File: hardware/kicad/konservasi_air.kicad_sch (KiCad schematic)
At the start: 29 parts, among them J1 ADS1115, J10 PUMP, J11 DC_IN_TERMINAL, J12 ESP_GPIO_LEFT, J13 ESP_GPIO_RIGHT, J2 DS18B20, J3 TDS, J4 TURBIDITY, J5 pH, J6 SERVO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

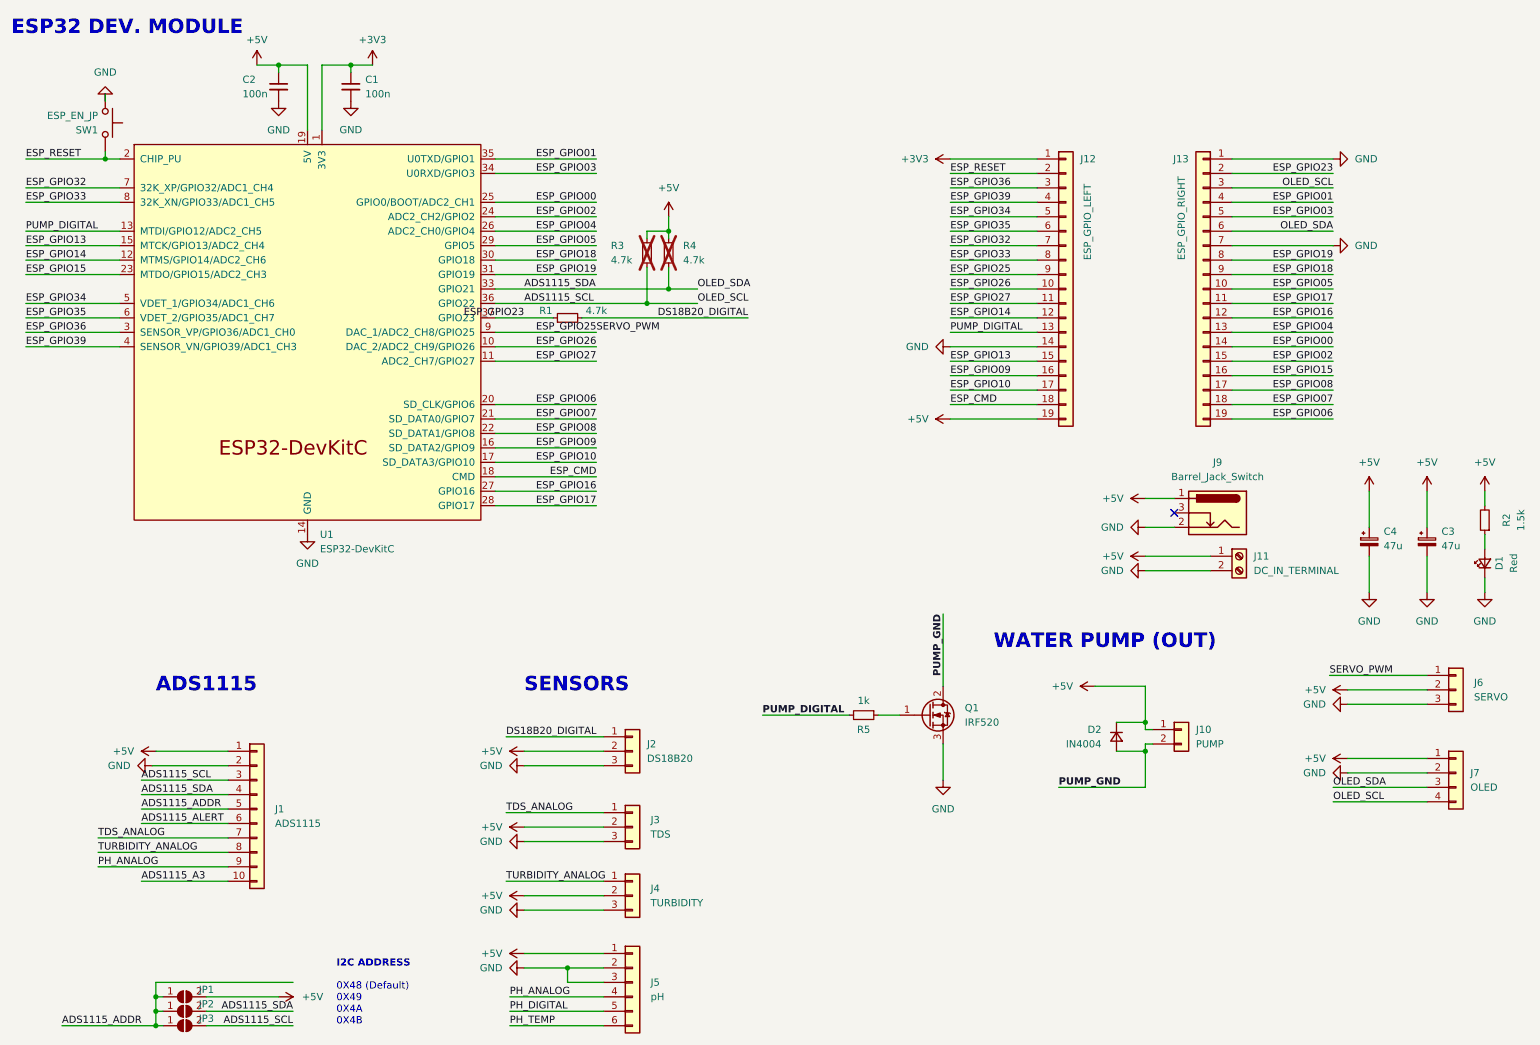
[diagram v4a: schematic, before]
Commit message: Fix Pullup for Temp Sensor
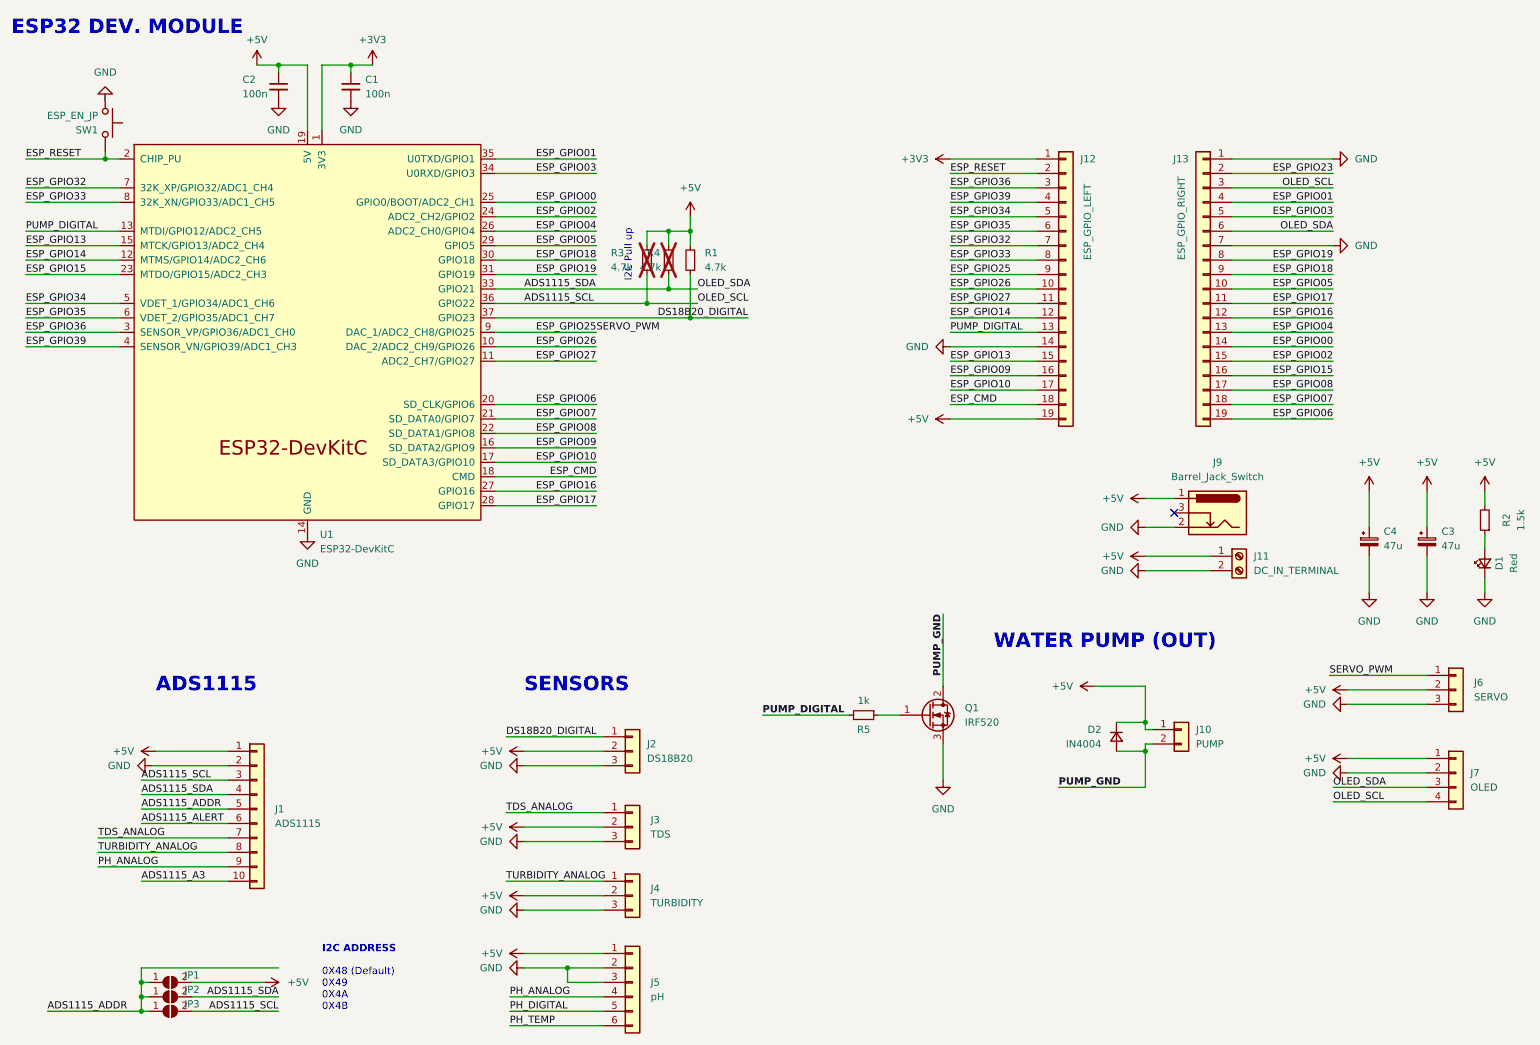
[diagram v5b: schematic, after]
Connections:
- net +5V: now also R1.2
- net DS18B20_DIGITAL: now also R1.1, U1.37 (GPIO23); no longer R1.2
- net ESP_GPIO23: no longer R1.1, U1.37 (GPIO23)
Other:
- note added: "I2C Pull up"
- moved on the sheet: JP1, JP2, JP3, R3, R4

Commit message: Update konservasi_air.kicad_sch
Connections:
- net ESP_GPIO23 is gone; now on net DS18B20_DIGITAL: J13.2 (Pin_2)
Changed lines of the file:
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@@
-    (effects (font (size 1.27 1.27)) (justify right bottom))
-  )
-  (label "ESP_GPIO23" (at 246.38 41.91 180) (fields_autoplaced)
     (effects (font (size 1.27 1.27)) (justify right bottom))
   )
@@
     (effects (font (size 1.27 1.27)) (justify right bottom))
   )
+  (label "DS18B20_DIGITAL" (at 246.38 41.91 180) (fields_autoplaced)
+    (effects (font (size 1.27 1.27)) (justify right bottom))
+  )
